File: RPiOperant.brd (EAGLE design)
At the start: 77 x 64 mm, 44 parts, among them IC1 74LS14N, IC2 MCP3202P, J1 RASPBERRYPI-40-PIN-GPIO_PTH_N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, J2 POWER_JACK, J3 POWER_JACK

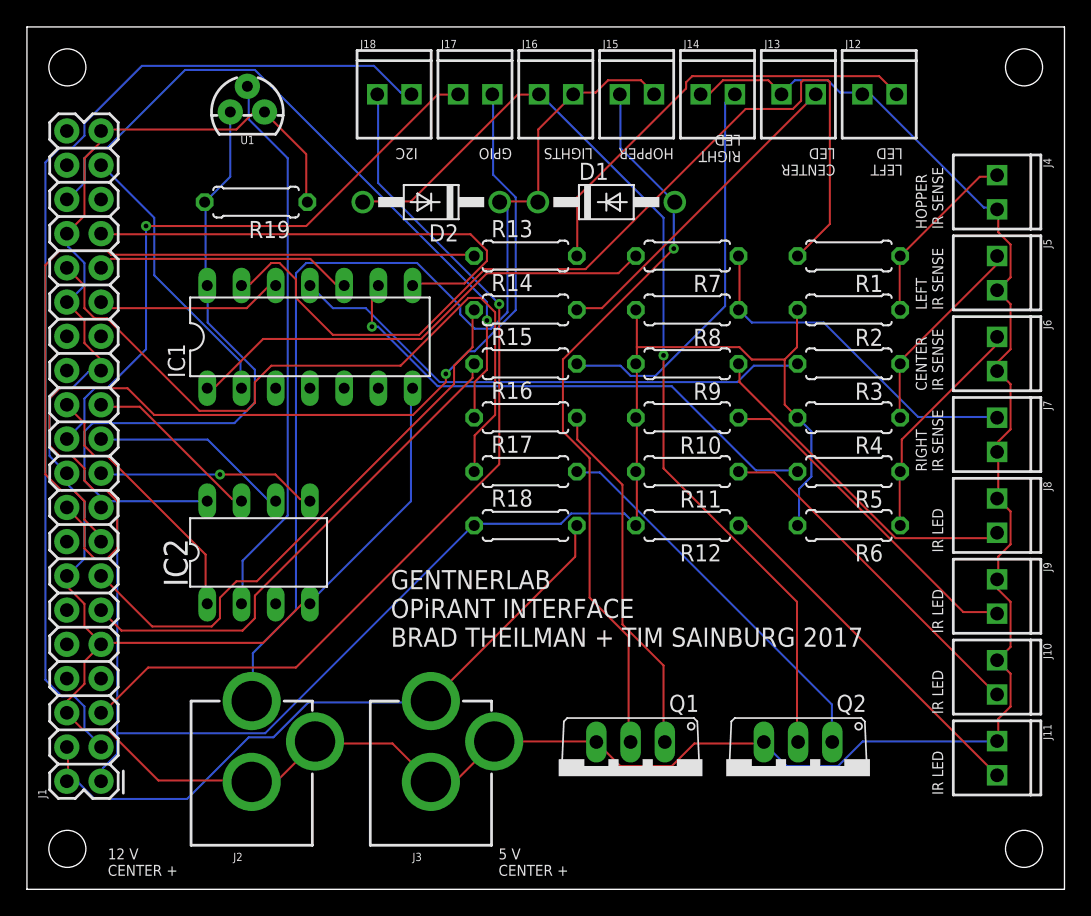
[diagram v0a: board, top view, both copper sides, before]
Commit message: update ground plane
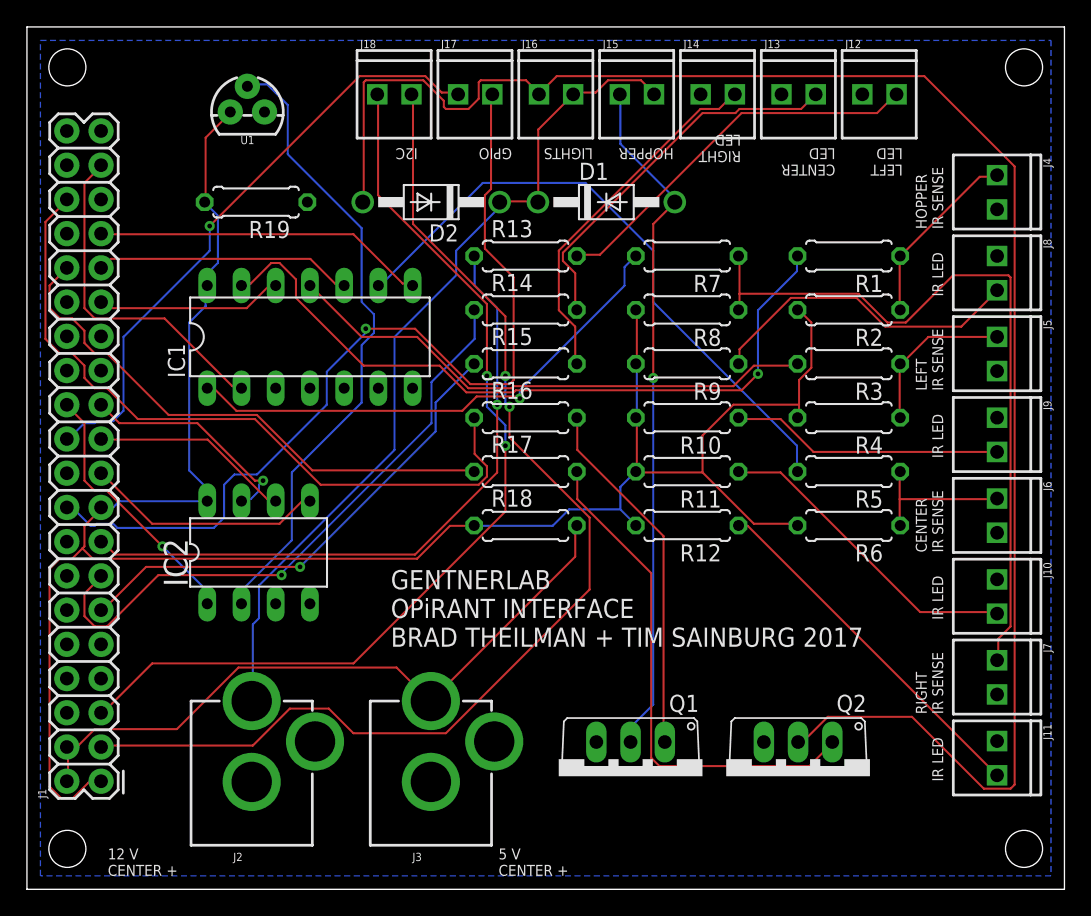
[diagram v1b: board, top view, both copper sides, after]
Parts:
- moved J7 18.0 mm to (72.0, 17.0)
- moved J8 18.0 mm to (72.0, 47.0)
- moved J6 12.0 mm to (72.0, 29.0)
- moved J9 12.0 mm to (72.0, 35.0)
- moved J10 6.00 mm to (72.0, 23.0)
- moved J5 6.00 mm to (72.0, 41.0)
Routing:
- net GND: track 259.5 -> 0.00 mm
- net N$26: track 72.5 -> 128.9 mm, vias 1 -> 0
- net N$11: track 26.5 -> 55.4 mm
- net 12V: track 79.3 -> 63.5 mm
- net N$6: track 70.0 -> 54.4 mm, vias 0 -> 1
- net N$28: track 54.4 -> 40.6 mm
- net N$3: track 36.2 -> 24.7 mm
- net N$35: track 77.0 -> 67.3 mm
- net N$27: track 28.9 -> 38.0 mm
- net N$37: track 77.2 -> 84.9 mm, vias 0 -> 2
- net N$10: track 39.3 -> 46.5 mm, vias 1 -> 0
- net N$33: track 41.1 -> 47.4 mm
- net N$20: track 55.2 -> 49.1 mm, vias 0 -> 1
- net N$9: track 17.0 -> 11.3 mm
- net N$14: track 25.2 -> 20.3 mm
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- added copper zone on layer 16, net GND

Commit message: update traces
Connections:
- new net +3V3: IC1.14, IC2.8, R10.2, R11.2, R12.2, R18.1, R19.2, R2.2, R4.2, R6.2, R8.2, R9.2, U1.1
- new net +5V: J3.PWR, R18.2
- net 3.3V: no longer IC1.14, IC2.8, R10.2, R11.2, R12.2, R18.1, R19.2, R2.2, R4.2, R6.2, R8.2, R9.2, U1.1
- net 5V: no longer J3.PWR, R18.2
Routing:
- net 3.3V: track 159.7 -> 21.4 mm
- net +3V3: track 0.00 -> 122.0 mm, vias 0 -> 1
- net N$26: track 128.9 -> 68.5 mm, vias 0 -> 2
- net 5V: track 50.7 -> 2.55 mm
- net N$28: track 40.6 -> 82.8 mm
- net N$3: track 24.7 -> 50.3 mm
- net N$37: track 84.9 -> 63.9 mm
- net N$6: track 54.4 -> 74.1 mm
- net +5V: track 0.00 -> 17.5 mm
- net N$25: track 53.8 -> 41.2 mm, vias 0 -> 1
- net N$36: track 71.1 -> 61.9 mm, vias 2 -> 0
- net N$10: track 46.5 -> 37.7 mm, vias 0 -> 1
- net N$31: track 14.9 -> 22.1 mm
- net N$22: track 36.5 -> 42.9 mm
- net N$20: track 49.1 -> 42.9 mm
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
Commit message: rework
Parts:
- removed IC2: MCP3202P, microchip:DIL8
- removed J1: RASPBERRYPI-40-PIN-GPIO_PTH_NO_SHROUD, SparkFun-Connectors:2X20
- removed J10, J11, J12, J13, J14, J15, J16, J17, J18, J4, J5, J6, J7, J8, J9: (no value), SparkFun-Connectors:1X02_2.54_SCREWTERM
- removed R13, R14, R15: 330, resistor:0207/7
- added IC3: MCP3008, adafruit:DIL16
- added SV1, SV2: (no value), con-lstb:MA20-2
- added X1: (no value), con-subd:F25HP
- moved R1 133.5 mm to (-72.4, 53.3), turned to 0 degrees
- moved R6 124.2 mm to (-58.4, 61.0), turned to 0 degrees
- moved R7 118.4 mm to (-68.6, 61.0), turned to 0 degrees
- moved R12 114.3 mm to (-58.4, 66.0), turned to 0 degrees
- moved R5 113.3 mm to (-48.3, 61.0), turned to 0 degrees
- moved R18 105.1 mm to (-58.4, 71.1)
- moved R11 103.4 mm to (-48.3, 66.0), turned to 0 degrees
- moved R4 102.4 mm to (-38.1, 61.0), turned to 0 degrees
- moved Q2 101.0 mm to (-30.5, 58.4), turned to 0 degrees
- moved R17 94.2 mm to (-48.3, 71.1)
- moved R10 92.5 mm to (-38.1, 66.0), turned to 0 degrees
- moved R3 91.6 mm to (-27.9, 61.0), turned to 0 degrees
- moved J2 90.3 mm to (-73.7, 1.27)
- moved R19 87.9 mm to (-68.6, 71.1), turned to 0 degrees
- moved D1 86.3 mm to (-43.2, 55.9)
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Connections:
- removed net 3.3V: J1.1, J1.17
- removed net 5V: J1.2, J1.4
- removed net N$1: IC1.12, J1.29
- removed net N$11: J7.P2, R7.1, R8.1
- removed net N$13: J8.P1, R9.1
- removed net N$14: J9.P1, R10.1
- removed net N$15: J10.P1, R11.1
- removed net N$16: J11.P1, R12.1
- removed net N$17: J12.P1, R13.2
- removed net N$18: J13.P1, R14.2
- removed net N$19: J14.P1, R15.2
- removed net N$2: IC1.10, J1.31
- removed net N$20: J1.15, R13.1
- removed net N$21: J1.13, R14.1
- removed net N$22: J1.11, R15.1
- removed net N$23: D1.A, J15.P2, Q1.2
- removed net N$25: J1.36, R16.1
- removed net N$26: D2.A, J16.P2, Q2.2
- removed net N$28: J1.32, R17.1
- removed net N$29: IC2.1, J1.24
- removed net N$3: IC1.8, J1.33
- removed net N$30: IC2.7, J1.23
- removed net N$31: IC2.6, J1.21
- removed net N$32: IC2.5, J1.19
- removed net N$33: IC2.2, U1.2
- removed net N$34: J1.22, J17.P2
- removed net N$35: J1.18, J17.P1
- removed net N$36: J1.5, J18.P2
- removed net N$37: J1.3, J18.P1
- removed net N$4: IC1.2, J1.37
- removed net N$5: J4.P2, R1.1, R2.1
- removed net N$7: J5.P2, R3.1, R4.1
- removed net N$9: J6.P2, R5.1, R6.1
- new net CE0: SV1.24
- new net CE1: IC3.10, SV1.26
- new net CENTER_IR: X1.11
- new net CENTER_LED: X1.8
- new net CENTER_PECK_GPIO: IC1.8, SV1.33
- new net CENTNER_IR: R5.1, R6.1
- new net GPIO2: SV1.3, X1.14
- new net GPIO20: X1.21
- new net GPIO21: X1.22
- new net GPIO23: X1.16
- new net GPIO24: X1.17
- new net GPIO25: X1.18
- new net GPIO3: SV1.5, X1.15
- new net GPIO4: SV1.7
- new net GPIO7: X1.20
- new net GPIO8: X1.19
- new net HOPPER: D1.A, Q1.2, X1.6
- new net HOPPER_IR: R1.1, R2.1, X1.13
- new net HOPPER_IR_GPIO: IC1.12, SV1.29
- new net HOPPER_TRIG_GPIO: R16.1, SV1.36
- new net HOUSE_LIGHTS: D2.A, Q2.2, X1.5
- new net LEFT_IR: R3.1, R4.1, X1.12
- new net LEFT_LED: X1.9
- new net LEFT_PECK_GPIO: IC1.10, SV1.31
- new net LIGHTS_TRIG_GPIO: R17.1, SV1.32
- new net MISO: IC3.12, SV1.21
- new net MOSI: IC3.11, SV1.19
- new net N$47: X1.4
- new net N$48: X1.3
- new net N$49: X1.2
- new net N$50: X1.1
- new net RIGHT_IR: R7.1, R8.1, X1.10
- new net RIGHT_LED: X1.7
- new net RIGHT_PECK_GPIO: IC1.2, SV1.37
- new net SCLK: IC3.13, SV1.23
- net +3V3: now also IC3.15, IC3.16; no longer IC2.8, U1.1
- net +5V: now also X1.25
- net 12V: now also X1.24; no longer J15.P1, J16.P1
- net GND: now also IC3.14, IC3.9, X1.23, X1.G1, X1.G2; no longer IC2.4, J1.14, J1.20, J1.25, J1.30, J1.34, J1.39, J1.6, J1.9, J10.P2, J11.P2, J12.P2, J13.P2, J14.P2, J4.P1, J5.P1, J6.P1, J7.P1, J8.P2, J9.P2, U1.3
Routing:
- net +3V3: track 122.0 -> 0.00 mm, vias 1 -> 0
- net N$28: track 82.8 -> 0.00 mm
- net N$6: track 74.1 -> 0.00 mm, vias 1 -> 0
- net N$26: track 68.5 -> 0.00 mm, vias 2 -> 0
- net N$35: track 68.3 -> 0.00 mm, vias 1 -> 0
- net 12V: track 64.2 -> 0.00 mm, vias 1 -> 0
- net N$37: track 63.9 -> 0.00 mm, vias 2 -> 0
- net N$36: track 61.9 -> 0.00 mm
- net N$23: track 57.2 -> 0.00 mm, vias 1 -> 0
- net N$11: track 55.4 -> 0.00 mm
- net N$21: track 50.3 -> 0.00 mm, vias 1 -> 0
- net N$3: track 50.3 -> 0.00 mm
- net N$34: track 44.9 -> 0.00 mm, vias 1 -> 0
- net N$33: track 43.6 -> 0.00 mm, vias 2 -> 0
- net N$20: track 42.9 -> 0.00 mm, vias 1 -> 0
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- removed copper zone on layer 16, net GND
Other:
- board size 77 x 64 mm -> 100 x 80 mm
- board text removed: "12 V CENTER +"
- board text removed: "5 V CENTER +"
- board text removed: "CENTER IR SENSE"
- board text removed: "CENTER LED"
- board text removed: "GENTNERLAB OPiRANT INTERFACE BRAD THEILMAN + TIM SAINBURG 2017"
- board text removed: "GPIO"
- board text removed: "HOPPER"
- board text removed: "HOPPER IR SENSE"
- board text removed: "I2C"
- board text removed: "IR LED"
- board text removed: "LEFT IR SENSE"
- board text removed: "LEFT LED"
- board text removed: "LIGHTS"
- board text removed: "RIGHT IR SENSE"
- board text removed: "RIGHT LED"

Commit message: new board
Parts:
- removed R10, R11, R12, R9: 330, resistor:0207/7
- added R13, R14: 1k, resistor:0207/7
- added R15, R20: 4.3, resistor:0207/7
- added R21, R22, R23: 330, resistor:0207/7
- moved SV2 175.8 mm to (82.5, 30.5), turned to 90 degrees
- moved R19 145.5 mm to (71.1, 30.5), turned to 180 degrees
- moved R7 134.6 mm to (59.7, 20.3)
- moved R18 134.3 mm to (71.1, 35.6)
- moved IC3 127.2 mm to (34.3, 29.2), turned to 270 degrees
- moved D2 124.9 mm to (62.2, 15.2)
- moved R6 123.3 mm to (59.7, 25.4)
- moved R17 123.2 mm to (71.1, 40.6)
- moved R16 121.0 mm to (71.1, 19.1)
- moved R5 112.2 mm to (59.7, 30.5)
- moved R1 107.0 mm to (34.3, 45.7), turned to 180 degrees
- moved SV1 105.4 mm to (5.08, 30.5), turned to 90 degrees
- moved Q2 105.2 mm to (61.0, 6.35), turned to 180 degrees
- moved R4 101.0 mm to (59.7, 35.6)
- moved D1 100.1 mm to (48.3, 15.2), turned to 180 degrees
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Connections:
- removed net GPIO23: X1.16
- removed net GPIO24: X1.17
- removed net N$47: X1.4
- removed net N$48: X1.3
- removed net N$49: X1.2
- removed net N$50: X1.1
- new net ADC0: IC3.1, X1.2
- new net ADC1: IC3.2, X1.1
- new net ADC2: IC3.3, X1.17
- new net ADC3: IC3.4
- new net ADC4: IC3.5, X1.16
- new net ADC5: IC3.6
- new net ADC6: IC3.7
- new net ADC7: IC3.8
- new net GPIO17: R23.1, SV1.11, SV2.11
- new net GPIO22: R21.1, SV1.15, SV2.15
- new net GPIO27: R22.2, SV1.13, SV2.13
- new net IR_1: R13.1, R15.1, X1.4
- new net IR_1_GPIO: IC1.4
- new net IR_2: R14.1, R20.1, X1.3
- new net IR_2_GPIO: IC1.6
- new net N$1: IC1.3, R13.2
- new net N$2: IC1.5, R14.2
- net +3V3: now also R15.2, R20.2; no longer R10.2, R11.2, R12.2, R9.2
- net CE0: now also SV2.24
- net CE1: now also SV2.26
- net CENTER_LED: now also R22.1
- net CENTER_PECK_GPIO: now also SV2.33
- net GND: now also SV1.14, SV1.20, SV1.25, SV1.30, SV1.34, SV1.39, SV1.6, SV1.9, SV2.14, SV2.20, SV2.25, SV2.30, SV2.34, SV2.39, SV2.6, SV2.9
- net GPIO2: now also SV2.3
- net GPIO3: now also SV2.5
- net GPIO4: now also SV2.7
- net HOPPER_IR_GPIO: now also SV2.29
- net HOPPER_TRIG_GPIO: now also SV2.36
- net LEFT_LED: now also R23.2
- net LEFT_PECK_GPIO: now also SV2.31
- net LIGHTS_TRIG_GPIO: now also SV2.32
- net MISO: now also SV2.21
- net MOSI: now also SV2.19
- net RIGHT_LED: now also R21.2
- net RIGHT_PECK_GPIO: now also SV2.37
- net SCLK: now also SV2.23
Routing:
- net GPIO3: track 0.00 -> 169.9 mm, vias 0 -> 2
- net GPIO2: track 0.00 -> 158.6 mm, vias 0 -> 2
- net GPIO22: track 0.00 -> 153.8 mm
- net GPIO27: track 0.00 -> 141.6 mm
- net CENTER_PECK_GPIO: track 0.00 -> 129.5 mm, vias 0 -> 1
- net HOPPER_TRIG_GPIO: track 0.00 -> 123.8 mm, vias 0 -> 2
- net LEFT_PECK_GPIO: track 0.00 -> 119.5 mm
- net RIGHT_PECK_GPIO: track 0.00 -> 116.2 mm
- net 12V: track 0.00 -> 114.1 mm
- net HOPPER_IR_GPIO: track 0.00 -> 112.8 mm
- net LIGHTS_TRIG_GPIO: track 0.00 -> 103.7 mm, vias 0 -> 1
- net MOSI: track 0.00 -> 100.7 mm
- net CE0: track 0.00 -> 99.9 mm, vias 0 -> 1
- net MISO: track 0.00 -> 98.6 mm, vias 0 -> 2
- net N$1: track 0.00 -> 94.1 mm, vias 0 -> 1
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- added copper zone on layer 16, net GND
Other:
- board size 100 x 80 mm -> 87.3 x 64.8 mm

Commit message: updates
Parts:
- removed U1: (no value), SparkFun-Sensors:TO-92
- moved R2 44.9 mm to (15.0, 41.0)
- moved R4 34.1 mm to (26.0, 41.0)
- moved R3 34.0 mm to (26.0, 45.0)
- moved R17 29.5 mm to (42.0, 36.0)
- moved R18 29.3 mm to (42.0, 32.0)
- moved R8 28.6 mm to (48.0, 41.0)
- moved R6 27.5 mm to (37.0, 41.0)
- moved R7 27.3 mm to (48.0, 45.0)
- moved R5 26.9 mm to (37.0, 45.0)
- moved R19 19.9 mm to (52.0, 36.0), turned to 0 degrees
- moved R1 19.3 mm to (15.0, 45.0)
- moved D2 18.4 mm to (44.0, 18.0), turned to 180 degrees
- moved R22 17.1 mm to (62.0, 32.0)
- moved R21 16.8 mm to (62.0, 36.0), turned to 0 degrees
- moved R15 14.1 mm to (52.0, 28.0)
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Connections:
- new net RPI_3.3V: SV1.1, SV1.17, SV2.1, SV2.17
- new net RPI_5V: SV1.2, SV1.4, SV2.2, SV2.4
- net IR_1_GPIO: now also SV1.16
- net IR_2_GPIO: now also SV1.18, SV2.18
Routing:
- net RPI_3.3V: track 0.00 -> 127.1 mm, vias 0 -> 1
- net RPI_5V: track 0.00 -> 77.5 mm
- net N$8: track 72.4 -> 25.3 mm
- net GPIO27: track 141.6 -> 101.7 mm, vias 0 -> 1
- net 12V: track 114.1 -> 76.7 mm, vias 0 -> 3
- net GPIO3: track 169.9 -> 132.9 mm
- net RIGHT_IR: track 44.7 -> 12.4 mm
- net GPIO22: track 153.8 -> 125.1 mm, vias 0 -> 2
- net LEFT_IR: track 17.5 -> 44.8 mm
- net N$10: track 60.0 -> 34.9 mm, vias 2 -> 0
- net LIGHTS_TRIG_GPIO: track 103.7 -> 79.0 mm, vias 1 -> 2
- net +5V: track 82.0 -> 59.9 mm
- net N$12: track 62.2 -> 83.0 mm, vias 2 -> 1
- net RIGHT_PECK_GPIO: track 116.2 -> 97.2 mm, vias 0 -> 2
- net HOPPER_IR: track 34.1 -> 52.8 mm
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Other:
- board size 87.3 x 64.8 mm -> 80 x 64 mm
- board text added: "GENTNER LAB OPiRANT INTERFACE BRAD THEILMAN + TIM SAINBURG"

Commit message: panel breakeout :
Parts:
- added R10, R11, R12, R9: 330, resistor:0207/7
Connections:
- removed net GPIO20: X1.21
- removed net GPIO21: X1.22
- removed net GPIO7: X1.20
- removed net GPIO8: X1.19
- new net HOPPER_IR_LED: R12.1, X1.19
- new net IR_LED_C: R10.1, X1.21
- new net IR_LED_L: R9.1, X1.22
- new net IR_LED_R: R11.1, X1.20
- net +3V3: now also R10.2, R11.2, R12.2, R9.2
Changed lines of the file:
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@@
 <element name="R22" library="resistor" library_urn="urn:adsk.eagle:library:348" package="0207/7" package3d_urn="urn:adsk.eagle:package:25942/1" value="330" x="62" y="32"/>
 <element name="R23" library="resistor" library_urn="urn:adsk.eagle:library:348" package="0207/7" package3d_urn="urn:adsk.eagle:package:25942/1" value="330" x="42" y="28"/>
+<element name="R9" library="resistor" library_urn="urn:adsk.eagle:library:348" package="0207/7" package3d_urn="urn:adsk.eagle:package:25942/1" value="330" x="2" y="-20"/>
+<element name="R10" library="resistor" library_urn="urn:adsk.eagle:library:348" package="0207/7" package3d_urn="urn:adsk.eagle:package:25942/1" value="330" x="2" y="-34"/>
+<element name="R11" library="resistor" library_urn="urn:adsk.eagle:library:348" package="0207/7" package3d_urn="urn:adsk.eagle:package:25942/1" value="330" x="2" y="-48"/>
+<element name="R12" library="resistor" library_urn="urn:adsk.eagle:library:348" package="0207/7" package3d_urn="urn:adsk.eagle:package:25942/1" value="330" x="2" y="-62"/>
 </elements>
 <signals>
@@
 <via x="37.2618" y="49.3776" extent="1-16" drill="0.35"/>
 <via x="37.4142" y="25.8318" extent="1-16" drill="0.35"/>
-</signal>
-<signal name="GPIO21">
-<contactref element="X1" pad="22"/>
-</signal>
-<signal name="GPIO20">
-<contactref element="X1" pad="21"/>
-</signal>
-<signal name="GPIO7">
-<contactref element="X1" pad="20"/>
-</signal>
-<signal name="GPIO8">
-<contactref element="X1" pad="19"/>
 </signal>
 <signal name="GPIO25">
@@
 <wire x1="51.7398" y1="40.9956" x2="51.81" y2="41" width="0.1524" layer="16"/>
 <wire x1="40.8432" y1="40.9956" x2="40.81" y2="41" width="0.1524" layer="16"/>
+<contactref element="R11" pad="2"/>
+<contactref element="R9" pad="2"/>
+<contactref element="R10" pad="2"/>
+<contactref element="R12" pad="2"/>
+<wire x1="5.81" y1="-48" x2="5.81" y2="-62" width="0" layer="19" extent="1-1"/>
+<wire x1="5.81" y1="-34" x2="5.81" y2="-48" width="0" layer="19" extent="1-1"/>
+<wire x1="5.81" y1="-20" x2="5.81" y2="-34" width="0" layer="19" extent="1-1"/>
+<wire x1="18.8214" y1="34.671" x2="5.81" y2="-20" width="0" layer="19" extent="16-16"/>
 </signal>
 <signal name="HOPPER_IR_GPIO">
@@
 <via x="7.3152" y="21.4122" extent="1-16" drill="0.35"/>
 </signal>
+<signal name="IR_LED_L">
+<contactref element="X1" pad="22"/>
+<contactref element="R9" pad="1"/>
+<wire x1="-1.81" y1="-20" x2="46.9088" y2="54.27" width="0" layer="19" extent="1-1"/>
+</signal>
+<signal name="IR_LED_C">
+<contactref element="X1" pad="21"/>
+<contactref element="R10" pad="1"/>
+<wire x1="-1.81" y1="-34" x2="44.1402" y2="54.27" width="0" layer="19" extent="1-1"/>
+</signal>
+<signal name="IR_LED_R">
+<contactref element="X1" pad="20"/>
+<contactref element="R11" pad="1"/>
+<wire x1="-1.81" y1="-48" x2="41.3716" y2="54.27" width="0" layer="19" extent="1-1"/>
+</signal>
+<signal name="HOPPER_IR_LED">
+<contactref element="X1" pad="19"/>
+<contactref element="R12" pad="1"/>
+<wire x1="-1.81" y1="-62" x2="38.6284" y2="54.27" width="0" layer="19" extent="1-1"/>
+</signal>
 </signals>
